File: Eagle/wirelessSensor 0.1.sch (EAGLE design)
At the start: 17 parts, among them U1 HDC1080, U2 PIC16F1823-X_SL, X1 22-23-2021

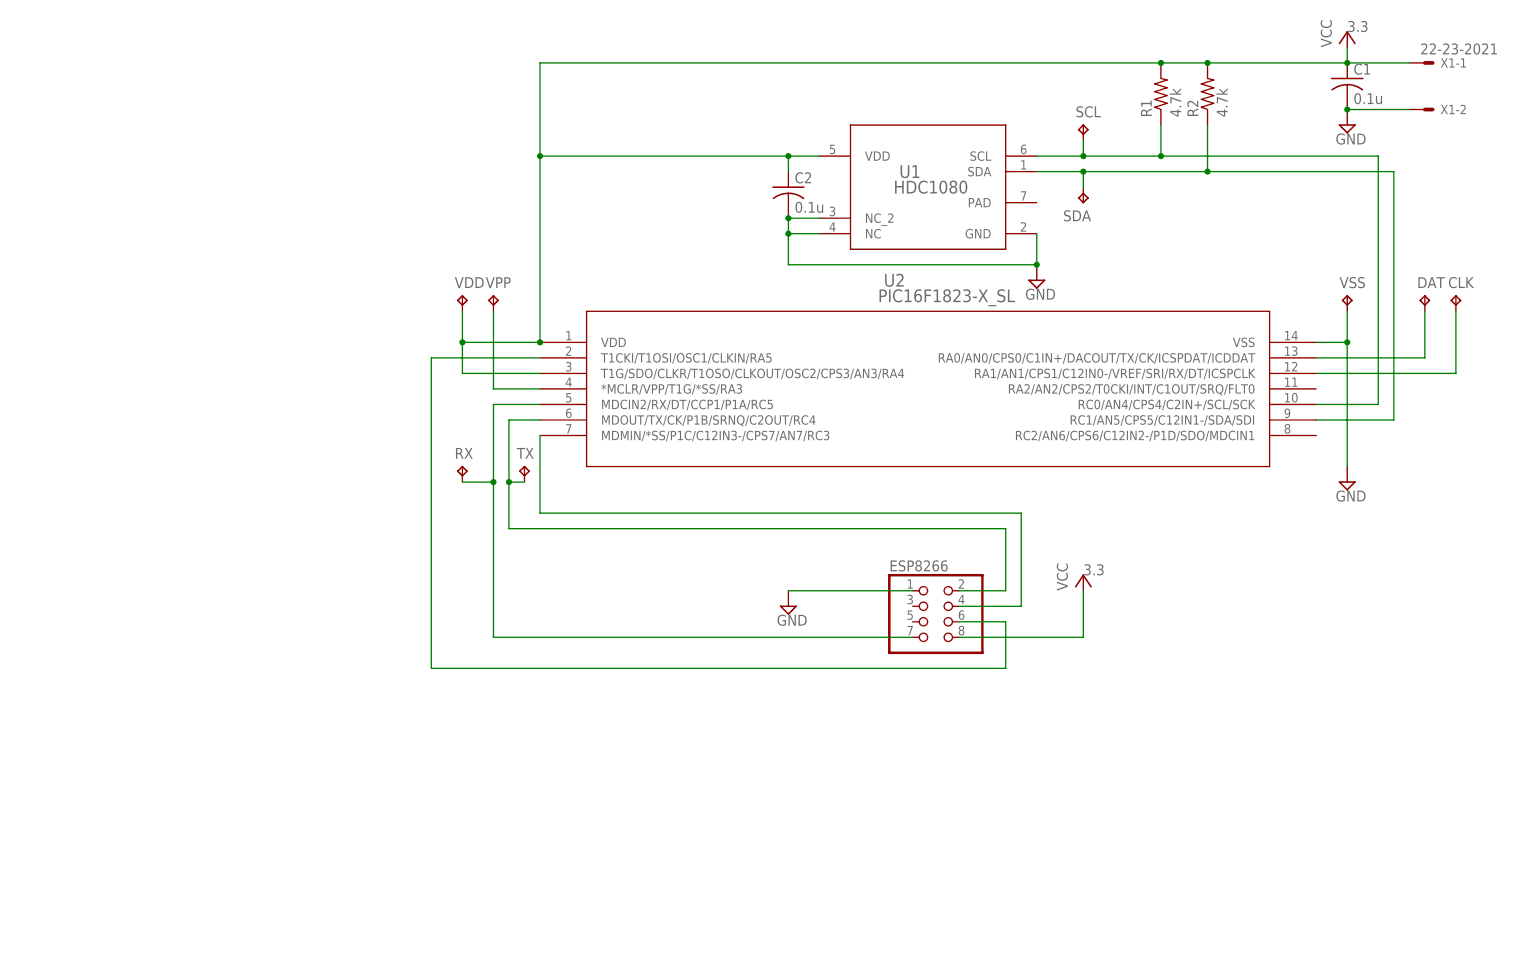
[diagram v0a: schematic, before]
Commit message: Changed .gitignore to match the directory changes, started cleaning up the layout
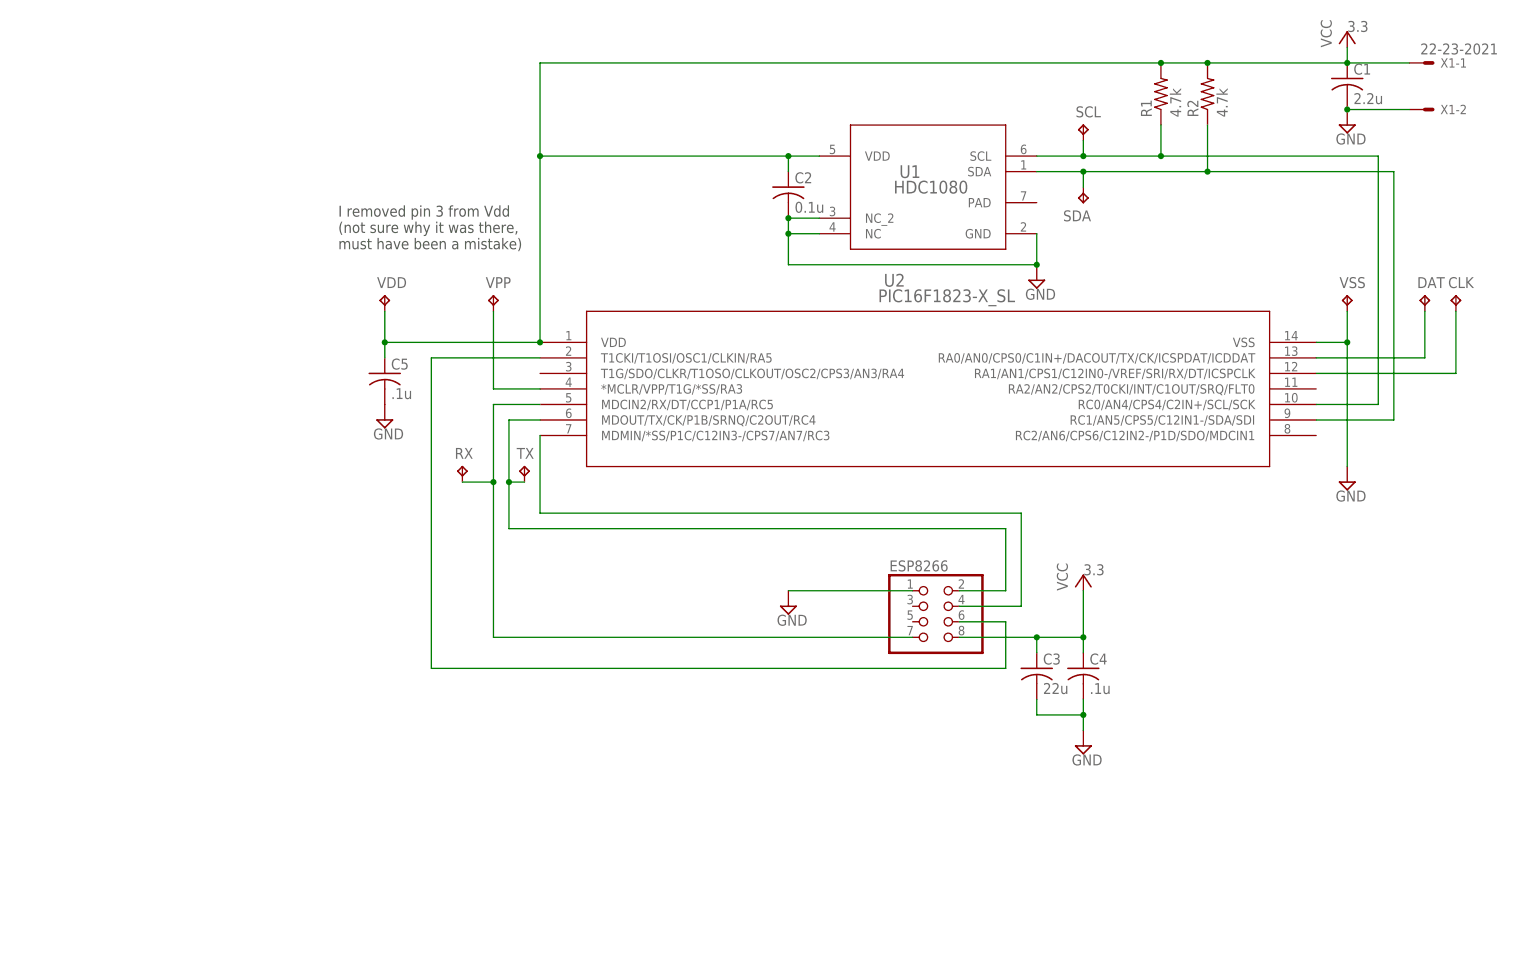
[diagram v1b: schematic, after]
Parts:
- added C3: 22u, rcl:C-USC0603K
- added C4, C5: .1u, rcl:C-USC0603K
- C1: value 0.1u -> 2.2u
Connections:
- net GND: now also C3.2, C4.2, C5.2
- net VCC: now also C3.1, C4.1, C5.1; no longer U2.T1G/SDO/CLKR/T1OSO/CLKOUT/OSC2/CPS3/AN3/RA4
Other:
- note added: "I removed pin 3 from Vdd (not sure why it was there, must have been a mistake)"
- moved on the sheet: VDD
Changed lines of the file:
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@@
 <part name="CLK" library="testpad" deviceset="TP" device="B1,27"/>
 <part name="X1" library="con-molex" deviceset="22-23-2021" device=""/>
-<part name="C1" library="rcl" deviceset="C-US" device="C0603" value="0.1u"/>
+<part name="C1" library="rcl" deviceset="C-US" device="C0603" value="2.2u"/>
 <part name="+3.1" library="supply1" deviceset="VCC" device="">
 <attribute name="VOLTAGE" value="3.3"/>
@@
 <part name="R1" library="rcl" deviceset="R-US_" device="R0603" value="4.7k"/>
 <part name="R2" library="rcl" deviceset="R-US_" device="R0603" value="4.7k"/>
+<part name="C3" library="rcl" deviceset="C-US" device="C0603K" value="22u"/>
+<part name="C4" library="rcl" deviceset="C-US" device="C0603K" value=".1u"/>
+<part name="C5" library="rcl" deviceset="C-US" device="C0603K" value=".1u"/>
+<part name="SUPPLY5" library="supply2" deviceset="GND" device=""/>
+<part name="SUPPLY6" library="supply2" deviceset="GND" device=""/>
 </parts>
 <sheets>
 <sheet>
 <plain>
+<text x="-96.52" y="17.78" size="1.778" layer="97">I removed pin 3 from Vdd
+(not sure why it was there,
+must have been a mistake)</text>
 </plain>
 <instances>
@@
 <instance part="SUPPLY2" gate="GND" x="17.78" y="12.7"/>
 <instance part="VPP" gate="G$1" x="-71.12" y="10.16"/>
-<instance part="VDD" gate="G$1" x="-76.2" y="10.16"/>
+<instance part="VDD" gate="G$1" x="-88.9" y="10.16"/>
 <instance part="VSS" gate="G$1" x="68.58" y="10.16"/>
 <instance part="DAT" gate="G$1" x="81.28" y="10.16"/>
@@
 <instance part="R1" gate="G$1" x="38.1" y="43.18" rot="R90"/>
 <instance part="R2" gate="G$1" x="45.72" y="43.18" rot="R90"/>
+<instance part="C3" gate="G$1" x="17.78" y="-50.8"/>
+<instance part="C4" gate="G$1" x="25.4" y="-50.8"/>
+<instance part="C5" gate="G$1" x="-88.9" y="-2.54"/>
+<instance part="SUPPLY5" gate="GND" x="25.4" y="-63.5"/>
+<instance part="SUPPLY6" gate="GND" x="-88.9" y="-10.16"/>
 </instances>
 <busses>
@@
 <wire x1="-63.5" y1="33.02" x2="-22.86" y2="33.02" width="0.1524" layer="91"/>
 <wire x1="-22.86" y1="33.02" x2="-17.78" y2="33.02" width="0.1524" layer="91"/>
-<wire x1="-63.5" y1="2.54" x2="-76.2" y2="2.54" width="0.1524" layer="91"/>
+<wire x1="-63.5" y1="2.54" x2="-88.9" y2="2.54" width="0.1524" layer="91"/>
 <junction x="-63.5" y="2.54"/>
 <pinref part="VDD" gate="G$1" pin="TP"/>
-<wire x1="-76.2" y1="2.54" x2="-76.2" y2="7.62" width="0.1524" layer="91"/>
-<pinref part="U2" gate="A" pin="T1G/SDO/CLKR/T1OSO/CLKOUT/OSC2/CPS3/AN3/RA4"/>
-<wire x1="-63.5" y1="-2.54" x2="-76.2" y2="-2.54" width="0.1524" layer="91"/>
-<wire x1="-76.2" y1="-2.54" x2="-76.2" y2="2.54" width="0.1524" layer="91"/>
-<junction x="-76.2" y="2.54"/>
+<wire x1="-88.9" y1="2.54" x2="-88.9" y2="7.62" width="0.1524" layer="91"/>
 <pinref part="C2" gate="G$1" pin="1"/>
 <wire x1="-22.86" y1="33.02" x2="-22.86" y2="30.48" width="0.1524" layer="91"/>
@@
 <wire x1="-63.5" y1="48.26" x2="38.1" y2="48.26" width="0.1524" layer="91"/>
 <junction x="38.1" y="48.26"/>
+<pinref part="C5" gate="G$1" pin="1"/>
+<wire x1="-88.9" y1="2.54" x2="-88.9" y2="0" width="0.1524" layer="91"/>
+<junction x="-88.9" y="2.54"/>
 </segment>
 <segment>
 <pinref part="ESP8266" gate="A" pin="8"/>
 <pinref part="+3.2" gate="VCC" pin="VCC"/>
-<wire x1="5.08" y1="-45.72" x2="25.4" y2="-45.72" width="0.1524" layer="91"/>
+<wire x1="5.08" y1="-45.72" x2="17.78" y2="-45.72" width="0.1524" layer="91"/>
+<wire x1="17.78" y1="-45.72" x2="25.4" y2="-45.72" width="0.1524" layer="91"/>
 <wire x1="25.4" y1="-45.72" x2="25.4" y2="-38.1" width="0.1524" layer="91"/>
+<pinref part="C4" gate="G$1" pin="1"/>
+<wire x1="25.4" y1="-45.72" x2="25.4" y2="-48.26" width="0.1524" layer="91"/>
+<junction x="25.4" y="-45.72"/>
+<pinref part="C3" gate="G$1" pin="1"/>
+<wire x1="17.78" y1="-48.26" x2="17.78" y2="-45.72" width="0.1524" layer="91"/>
+<junction x="17.78" y="-45.72"/>
 </segment>
 </net>
@@
 <wire x1="-22.86" y1="-38.1" x2="-2.54" y2="-38.1" width="0.1524" layer="91"/>
 </segment>
+<segment>
+<pinref part="C3" gate="G$1" pin="2"/>
+<wire x1="17.78" y1="-55.88" x2="17.78" y2="-58.42" width="0.1524" layer="91"/>
+<wire x1="17.78" y1="-58.42" x2="25.4" y2="-58.42" width="0.1524" layer="91"/>
+<pinref part="C4" gate="G$1" pin="2"/>
+<wire x1="25.4" y1="-58.42" x2="25.4" y2="-55.88" width="0.1524" layer="91"/>
+<pinref part="SUPPLY5" gate="GND" pin="GND"/>
+<wire x1="25.4" y1="-58.42" x2="25.4" y2="-60.96" width="0.1524" layer="91"/>
+<junction x="25.4" y="-58.42"/>
+</segment>
+<segment>
+<pinref part="C5" gate="G$1" pin="2"/>
+<pinref part="SUPPLY6" gate="GND" pin="GND"/>
+</segment>
 </net>
 <net name="N$2" class="0">
@@
 </schematic>
 </drawing>
+<compatibility>
+<note version="6.3" minversion="6.2.2" severity="warning">
+Since Version 6.2.2 text objects can contain more than one line,
+which will not be processed correctly with this version.
+</note>
+</compatibility>
 </eagle>

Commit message: Updated the layout a bit, should be ready for review/close to ready for order
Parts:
- added LED1: (no value), led:LEDCHIP-LED0603
- added R3: 330, rcl:R-US_R0603
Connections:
- new net N$10: LED1.A, U2.RA2/AN2/CPS2/T0CKI/INT/C1OUT/SRQ/FLT0
- new net N$11: LED1.C, R3.2
- net GND: now also R3.1
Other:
- note added: "HDC1080 NC can be floating or GND"
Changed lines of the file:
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@@
 <part name="SUPPLY5" library="supply2" deviceset="GND" device=""/>
 <part name="SUPPLY6" library="supply2" deviceset="GND" device=""/>
+<part name="LED1" library="led" deviceset="LED" device="CHIP-LED0603"/>
+<part name="R3" library="rcl" deviceset="R-US_" device="R0603" value="330"/>
 </parts>
 <sheets>
 <sheet>
 <plain>
-<text x="-96.52" y="17.78" size="1.778" layer="97">I removed pin 3 from Vdd
+<text x="-96.52" y="15.24" size="1.27" layer="97">I removed pin 3 from Vdd
 (not sure why it was there,
 must have been a mistake)</text>
+<text x="-12.7" y="40.64" size="1.27" layer="97">HDC1080 NC can be floating or GND</text>
 </plain>
 <instances>
 <instance part="U1" gate="A" x="0" y="27.94"/>
 <instance part="U2" gate="A" x="0" y="-5.08"/>
-<instance part="SUPPLY1" gate="GND" x="68.58" y="-20.32"/>
+<instance part="SUPPLY1" gate="GND" x="68.58" y="-25.4"/>
 <instance part="SUPPLY2" gate="GND" x="17.78" y="12.7"/>
 <instance part="VPP" gate="G$1" x="-71.12" y="10.16"/>
@@
 <instance part="SUPPLY5" gate="GND" x="25.4" y="-63.5"/>
 <instance part="SUPPLY6" gate="GND" x="-88.9" y="-10.16"/>
+<instance part="LED1" gate="G$1" x="88.9" y="-7.62"/>
+<instance part="R3" gate="G$1" x="88.9" y="-15.24" rot="R90"/>
 </instances>
 <busses>
@@
 <wire x1="63.5" y1="2.54" x2="68.58" y2="2.54" width="0.1524" layer="91"/>
 <pinref part="SUPPLY1" gate="GND" pin="GND"/>
-<wire x1="68.58" y1="2.54" x2="68.58" y2="-17.78" width="0.1524" layer="91"/>
+<wire x1="68.58" y1="2.54" x2="68.58" y2="-22.86" width="0.1524" layer="91"/>
 <pinref part="VSS" gate="G$1" pin="TP"/>
 <wire x1="68.58" y1="2.54" x2="68.58" y2="7.62" width="0.1524" layer="91"/>
 <junction x="68.58" y="2.54"/>
+<wire x1="68.58" y1="-22.86" x2="88.9" y2="-22.86" width="0.1524" layer="91"/>
+<junction x="68.58" y="-22.86"/>
+<pinref part="R3" gate="G$1" pin="1"/>
+<wire x1="88.9" y1="-22.86" x2="88.9" y2="-20.32" width="0.1524" layer="91"/>
 </segment>
 <segment>
@@
 </segment>
 </net>
+<net name="N$10" class="0">
+<segment>
+<pinref part="U2" gate="A" pin="RA2/AN2/CPS2/T0CKI/INT/C1OUT/SRQ/FLT0"/>
+<wire x1="63.5" y1="-5.08" x2="88.9" y2="-5.08" width="0.1524" layer="91"/>
+<pinref part="LED1" gate="G$1" pin="A"/>
+</segment>
+</net>
+<net name="N$11" class="0">
+<segment>
+<pinref part="LED1" gate="G$1" pin="C"/>
+<pinref part="R3" gate="G$1" pin="2"/>
+<wire x1="88.9" y1="-10.16" x2="88.9" y2="-12.7" width="0.1524" layer="91"/>
+</segment>
+</net>
